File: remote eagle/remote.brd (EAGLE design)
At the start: 36.8 x 36.8 mm, 12 parts, among them U1 BLE112-A

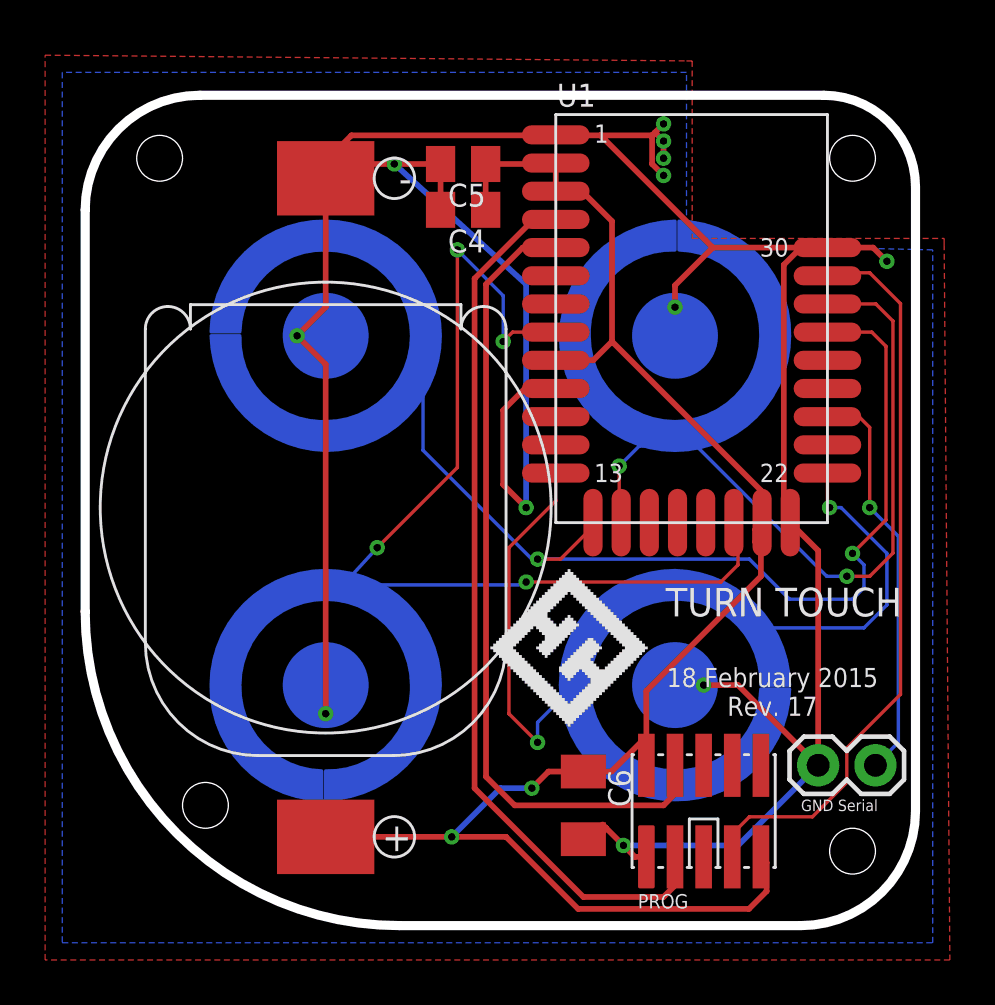
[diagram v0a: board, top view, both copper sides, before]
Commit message: Revision 18. Adding south dual-holes for orientation.
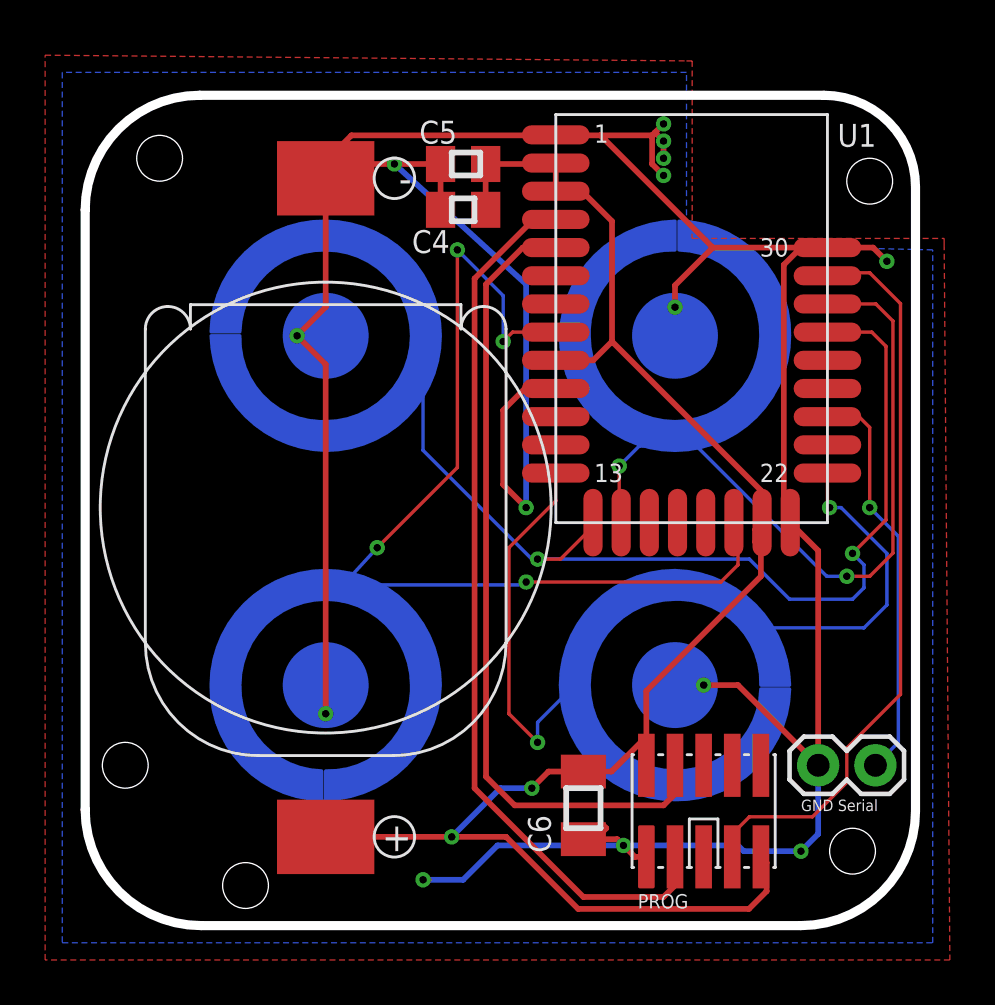
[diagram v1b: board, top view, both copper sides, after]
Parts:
- moved LOGO 13.2 mm to (7.62, 0.76), flipped to the bottom
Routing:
- net GND: track 146.7 -> 159.3 mm, vias 8 -> 10
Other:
- outline, holes or cut-outs redrawn
- board text added: "23 March 2015 Rev. 18"
- board text removed: "18 February 2015 Rev. 17"
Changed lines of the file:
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@@
 <layer number="22" name="bPlace" color="7" fill="1" visible="yes" active="yes"/>
 <layer number="23" name="tOrigins" color="15" fill="1" visible="yes" active="yes"/>
-<layer number="24" name="bOrigins" color="15" fill="1" visible="no" active="yes"/>
+<layer number="24" name="bOrigins" color="15" fill="1" visible="yes" active="yes"/>
 <layer number="25" name="tNames" color="7" fill="1" visible="yes" active="yes"/>
 <layer number="26" name="bNames" color="7" fill="1" visible="yes" active="yes"/>
@@
 <board>
 <plain>
-<text x="30.48" y="11.43" size="0.85" layer="25" font="vector" rot="SR0" align="top-center">18 February 2015
-Rev. 17</text>
-<text x="30.988" y="14.986" size="1.27" layer="25" font="vector" rot="SR0" align="top-center">TURN TOUCH</text>
+<text x="4.064" y="18.288" size="0.85" layer="26" font="vector" rot="SMR270" align="top-center">23 March 2015
+Rev. 18</text>
+<text x="1.27" y="18.288" size="1.27" layer="26" font="vector" rot="SMR270" align="top-center">TURN TOUCH</text>
 <text x="31.75" y="5.08" size="0.508" layer="25">GND Serial</text>
 <hole x="3.302" y="34.036" drill="2.032"/>
 <hole x="34.036" y="3.302" drill="2.032"/>
-<hole x="34.036" y="34.036" drill="2.032"/>
-<hole x="5.334" y="5.334" drill="2.032"/>
-<wire x1="0" y1="31.75" x2="0" y2="13.923740625" width="0.4064" layer="20"/>
-<wire x1="0" y1="13.923740625" x2="13.923740625" y2="0" width="0.4064" layer="20" curve="90"/>
-<wire x1="13.923740625" y1="0" x2="31.75" y2="0" width="0.4064" layer="20"/>
+<hole x="34.798" y="33.02" drill="2.032"/>
+<hole x="1.778" y="7.112" drill="2.032"/>
+<wire x1="0" y1="31.75" x2="0" y2="5.14310625" width="0.4064" layer="20"/>
+<wire x1="0" y1="5.14310625" x2="5.14310625" y2="0" width="0.4064" layer="20" curve="90"/>
+<wire x1="5.14310625" y1="0" x2="31.75" y2="0" width="0.4064" layer="20"/>
 <wire x1="31.75" y1="0" x2="36.83" y2="5.08" width="0.4064" layer="20" curve="90"/>
 <wire x1="36.83" y1="5.08" x2="36.83" y2="32.766" width="0.4064" layer="20"/>
@@
 <wire x1="32.766" y1="36.83" x2="5.08" y2="36.83" width="0.4064" layer="20"/>
 <wire x1="5.08" y1="36.83" x2="0" y2="31.75" width="0.4064" layer="20" curve="90"/>
+<hole x="7.112" y="1.778" drill="2.032"/>
+<wire x1="16.256" y1="34.29" x2="17.526" y2="34.29" width="0.254" layer="21"/>
+<wire x1="17.526" y1="34.29" x2="17.526" y2="33.274" width="0.254" layer="21"/>
+<wire x1="17.526" y1="33.274" x2="16.256" y2="33.274" width="0.254" layer="21"/>
+<wire x1="16.256" y1="33.274" x2="16.256" y2="34.29" width="0.254" layer="21"/>
+<wire x1="16.256" y1="32.258" x2="17.272" y2="32.258" width="0.254" layer="21"/>
+<wire x1="17.272" y1="32.258" x2="17.272" y2="31.242" width="0.254" layer="21"/>
+<wire x1="17.272" y1="31.242" x2="16.256" y2="31.242" width="0.254" layer="21"/>
+<wire x1="16.256" y1="31.242" x2="16.256" y2="32.258" width="0.254" layer="21"/>
+<wire x1="21.336" y1="6.096" x2="22.86" y2="6.096" width="0.254" layer="21"/>
+<wire x1="22.86" y1="6.096" x2="22.86" y2="4.318" width="0.254" layer="21"/>
+<wire x1="22.86" y1="4.318" x2="21.336" y2="4.318" width="0.254" layer="21"/>
+<wire x1="21.336" y1="4.318" x2="21.336" y2="6.096" width="0.254" layer="21"/>
 </plain>
 <attributes>
@@
 </autorouter>
 <elements>
-<element name="LOGO" library="remote" package="LOGO" value="" x="18.034" y="8.89"/>
+<element name="LOGO" library="remote" package="LOGO" value="" x="7.62" y="0.762" rot="MR0"/>
 <element name="U$6" library="remote" package="20MMCOINCELL" value="COINCELLHOLDER" x="10.668" y="18.542" rot="R180"/>
 <element name="JP2" library="SparkFun-Connectors" package="1X02" value="Serial" x="32.512" y="7.112" smashed="yes"/>
@@
 <attribute name="NAME" x="24.511" y="0.762" size="0.635" layer="25" font="vector" ratio="16"/>
 </element>
-<element name="U1" library="sf-bluegiga" package="BLE112-A" value="BLE112-A" x="26.924" y="26.924"/>
-<element name="C4" library="resistor" package="C0805K" value="1uF" x="16.764" y="31.75" rot="R180"/>
-<element name="C5" library="resistor" package="C0805K" value="1uF" x="16.764" y="33.782" rot="R180"/>
-<element name="C6" library="resistor" package="C1206K" value="100uF" x="22.098" y="5.334" rot="R270"/>
+<element name="U1" library="sf-bluegiga" package="BLE112-A" value="BLE112-A" x="26.924" y="26.924" smashed="yes">
+<attribute name="NAME" x="33.37" y="34.546" size="1.016" layer="25" rot="SR0"/>
+<attribute name="VALUE" x="26.924" y="36.324" size="1.016" layer="27" rot="SR0"/>
+</element>
+<element name="C4" library="resistor" package="C0805K" value="1uF" x="16.764" y="31.75" smashed="yes" rot="R180">
+<attribute name="NAME" x="14.494" y="29.831" size="1.016" layer="25"/>
+</element>
+<element name="C5" library="resistor" package="C0805K" value="1uF" x="16.764" y="33.782" smashed="yes" rot="R180">
+<attribute name="NAME" x="16.494" y="35.701" size="1.016" layer="25" rot="R180"/>
+</element>
+<element name="C6" library="resistor" package="C1206K" value="100uF" x="22.098" y="5.334" smashed="yes" rot="R270">
+<attribute name="NAME" x="19.642" y="4.902" size="1.016" layer="25" rot="R270"/>
+</element>
 <element name="U$1" library="remote" package="DOME-M-SERIES" value="SNAPTRON-DOME" x="26.162" y="26.162" rot="MR0"/>
 <element name="U$2" library="remote" package="DOME-M-SERIES" value="SNAPTRON-DOME" x="10.668" y="26.162" rot="MR270"/>
@@
 <contactref element="C5" pad="2"/>
 <contactref element="C4" pad="2"/>
-<polygon width="0.4064" layer="16" spacing="0.762" pour="hatch">
+<polygon width="0.4064" layer="16" spacing="0.762">
 <vertex x="-1.016" y="-0.762"/>
 <vertex x="37.592" y="-0.762"/>
@@
 <vertex x="-1.016" y="37.846"/>
 </polygon>
-<polygon width="0.4064" layer="1" spacing="0.762" pour="hatch">
+<polygon width="0.4064" layer="1" spacing="0.762">
 <vertex x="-1.778" y="38.608"/>
 <vertex x="26.67" y="38.354"/>
@@
 <via x="23.876" y="3.556" extent="1-16" drill="0.3302"/>
 <wire x1="23.876" y1="3.556" x2="28.956" y2="3.556" width="0.254" layer="16"/>
-<wire x1="28.956" y1="3.556" x2="32.512" y2="7.112" width="0.254" layer="16"/>
 <wire x1="32.512" y1="7.112" x2="32.512" y2="16.636" width="0.254" layer="1"/>
 <wire x1="32.512" y1="16.636" x2="31.274" y2="17.874" width="0.254" layer="1"/>
@@
 <wire x1="30.988" y1="18.16" x2="31.274" y2="17.874" width="0.254" layer="1"/>
 <wire x1="22.948" y1="4.484" x2="23.114" y2="4.318" width="0.254" layer="1"/>
-<wire x1="23.114" y1="4.318" x2="23.876" y2="3.556" width="0.254" layer="1"/>
 <wire x1="15.764" y1="33.782" x2="15.764" y2="31.75" width="0.254" layer="1"/>
 <wire x1="15.764" y1="33.782" x2="13.716" y2="33.782" width="0.254" layer="1"/>
@@
 <contactref element="U$4" pad="P$1"/>
 <wire x1="26.162" y1="10.668" x2="27.432" y2="10.668" width="0.254" layer="16"/>
-<wire x1="10.668" y1="33.909" x2="11.3665" y2="34.6075" width="0.254" layer="1"/>
-<wire x1="11.3665" y1="34.6075" x2="11.811" y2="35.052" width="0.254" layer="1"/>
+<wire x1="10.668" y1="33.909" x2="11.811" y2="35.052" width="0.254" layer="1"/>
 <wire x1="10.668" y1="33.655" x2="10.541" y2="33.782" width="0.254" layer="1"/>
 <wire x1="10.668" y1="27.432" x2="9.398" y2="26.162" width="0.254" layer="1"/>
@@
 <wire x1="10.668" y1="33.147" x2="10.668" y2="27.432" width="0.254" layer="1"/>
 <wire x1="10.541" y1="33.782" x2="10.668" y2="33.909" width="0.254" layer="1"/>
+<wire x1="32.512" y1="7.112" x2="32.512" y2="4.064" width="0.254" layer="16"/>
+<wire x1="32.512" y1="4.064" x2="31.75" y2="3.302" width="0.254" layer="16"/>
+<via x="31.75" y="3.302" extent="1-16" drill="0.3302"/>
+<wire x1="31.75" y1="3.302" x2="29.21" y2="3.302" width="0.254" layer="16"/>
+<wire x1="29.21" y1="3.302" x2="28.956" y2="3.556" width="0.254" layer="16"/>
+<wire x1="23.876" y1="3.556" x2="18.288" y2="3.556" width="0.254" layer="16"/>
+<wire x1="18.288" y1="3.556" x2="16.764" y2="2.032" width="0.254" layer="16"/>
+<wire x1="16.764" y1="2.032" x2="14.986" y2="2.032" width="0.254" layer="16"/>
+<via x="14.986" y="2.032" extent="1-16" drill="0.3302"/>
+<wire x1="14.986" y1="2.032" x2="15.24" y2="2.032" width="0.254" layer="1"/>
+<wire x1="22.098" y1="3.834" x2="23.598" y2="3.834" width="0.254" layer="1"/>
+<wire x1="23.598" y1="3.834" x2="23.876" y2="3.556" width="0.254" layer="1"/>
 </signal>
 <signal name="N$1">

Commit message: Cutting up the PCB to fit into the remodeled enclosure. Needs holding pegs.
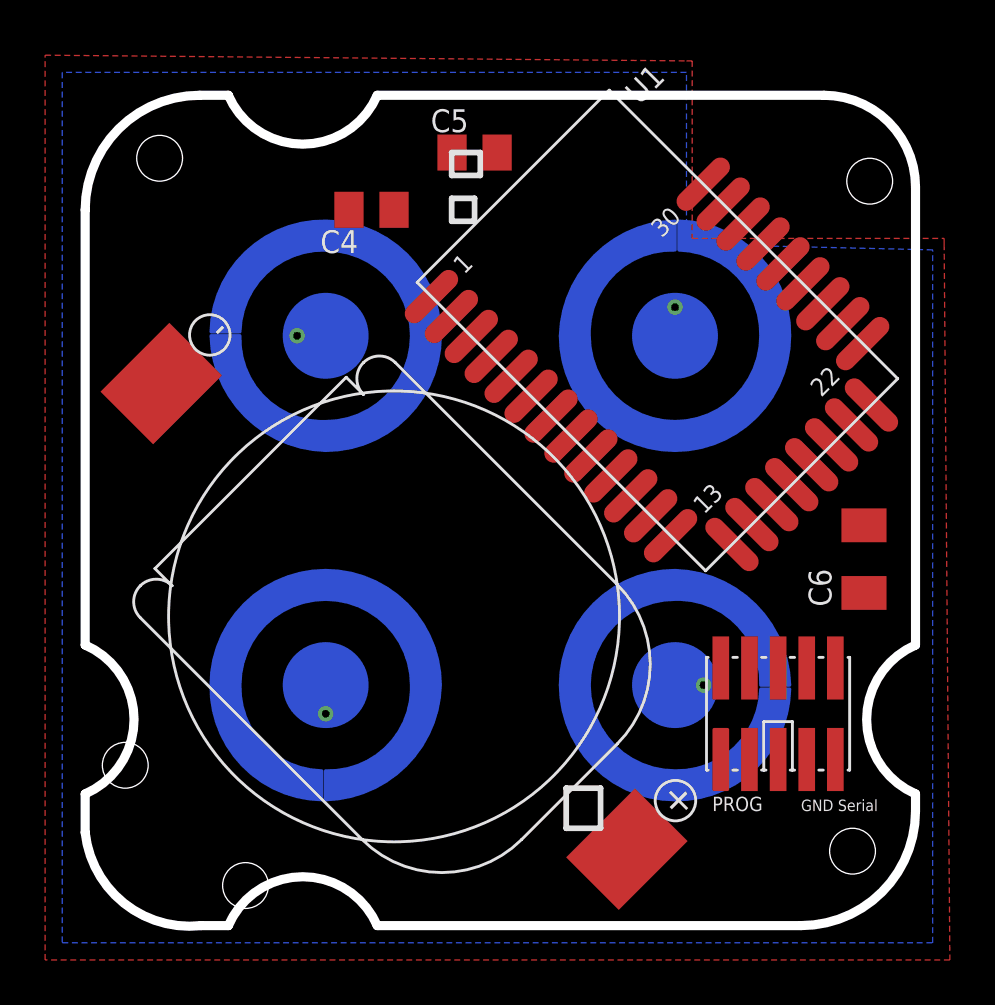
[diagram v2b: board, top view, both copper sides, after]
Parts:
- removed JP2: Serial, SparkFun-Connectors:1X02
- moved C6 16.6 mm to (34.5, 16.3)
- moved U$6 5.70 mm to (13.7, 13.7), turned to 225 degrees
- moved PROG 5.44 mm to (30.7, 9.40)
- moved C4 4.06 mm to (12.7, 31.8)
- moved U1 1.61 mm to (25.4, 26.4), turned to 45 degrees
- moved C5 0.72 mm to (17.3, 34.3)
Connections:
- net GND: no longer JP2.1
- net SERIAL: no longer JP2.2
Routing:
- net GND: track 159.3 -> 0.00 mm, vias 10 -> 0
- net 3.3V: track 75.1 -> 0.00 mm, vias 2 -> 0
- net BUTTON2: track 46.0 -> 0.00 mm, vias 2 -> 0
- net BUTTON4: track 45.7 -> 0.00 mm, vias 4 -> 0
- net BUTTON3: track 41.2 -> 0.00 mm, vias 2 -> 0
- net P2_2: track 40.5 -> 0.00 mm
- net P2_1: track 36.0 -> 0.00 mm
- net RESET: track 33.1 -> 0.00 mm
- net BUTTON1: track 32.4 -> 0.00 mm, vias 2 -> 0
- net SERIAL: track 18.0 -> 0.00 mm, vias 1 -> 0
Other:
- board size 36.8 x 36.8 mm -> 36.8 x 36.9 mm

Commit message: Revision 19 of the pcb, shaped to fit revision 9 of the enclosure (solidworks).
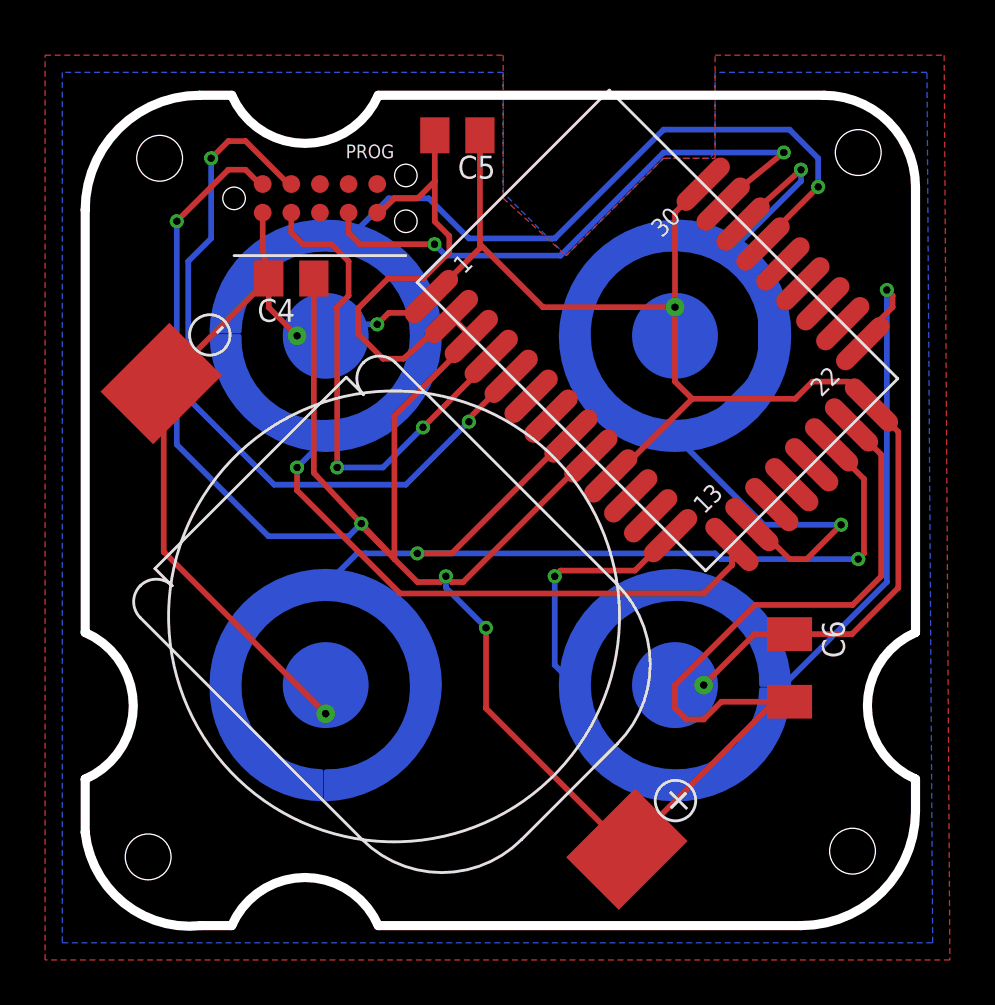
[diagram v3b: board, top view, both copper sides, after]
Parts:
- PROG: value CONN_5-2-FTSH-V -> TC2050-MCP-NL; device pel_misc:FTSH-105-DV -> TC2050:TC2030-MCP-NL
- moved PROG 33.2 mm to (6.60, 32.3)
- moved LOGO 20.1 mm to (21.8, 15.0)
- moved C6 5.85 mm to (31.2, 11.4), turned to 90 degrees
- moved C4 4.68 mm to (9.14, 28.7)
- moved C5 1.08 mm to (16.5, 35.1), turned to 0 degrees
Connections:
- net 3.3V: now also PROG.10, PROG.5; no longer PROG.2, PROG.9
- net P2_1: now also PROG.9; no longer PROG.4
- net P2_2: now also PROG.2; no longer PROG.3
- net RESET: now also PROG.4; no longer PROG.7
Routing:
- net 3.3V: track 0.00 -> 135.4 mm, vias 0 -> 4
- net GND: track 0.00 -> 102.2 mm, vias 0 -> 1
- net BUTTON2: track 0.00 -> 68.6 mm, vias 0 -> 2
- net BUTTON3: track 0.00 -> 47.9 mm, vias 0 -> 2
- net BUTTON4: track 0.00 -> 39.0 mm, vias 0 -> 2
- net P2_1: track 0.00 -> 33.7 mm, vias 0 -> 2
- net BUTTON1: track 0.00 -> 33.2 mm, vias 0 -> 2
- net RESET: track 0.00 -> 26.1 mm, vias 0 -> 2
- net P2_2: track 0.00 -> 22.3 mm, vias 0 -> 2
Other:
- outline, holes or cut-outs redrawn
- board text added: "5 June 2015 Rev. 19"
- board text removed: "23 March 2015 Rev. 18"
- board text removed: "GND Serial"
